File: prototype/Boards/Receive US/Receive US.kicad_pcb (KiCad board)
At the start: 2 copper layers, 37.1 x 26 mm, 37 parts, among them J1 Header, Q1 BC848BLT3G, U1 TLV9052SIDGSR, U2 TLV9052SIDGSR

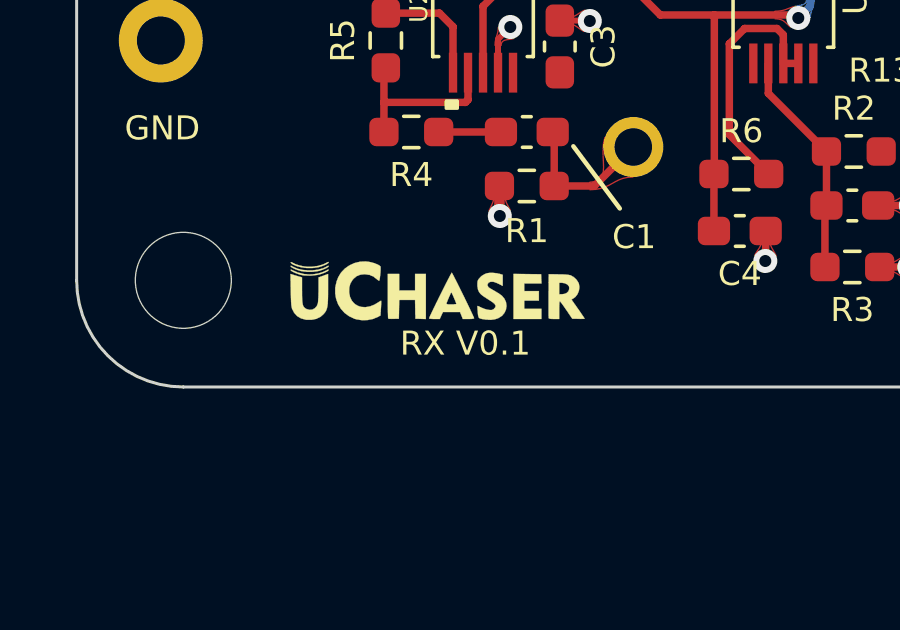
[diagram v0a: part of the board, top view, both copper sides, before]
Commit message: Update logo on receiver board; add new logo footprint & symbol
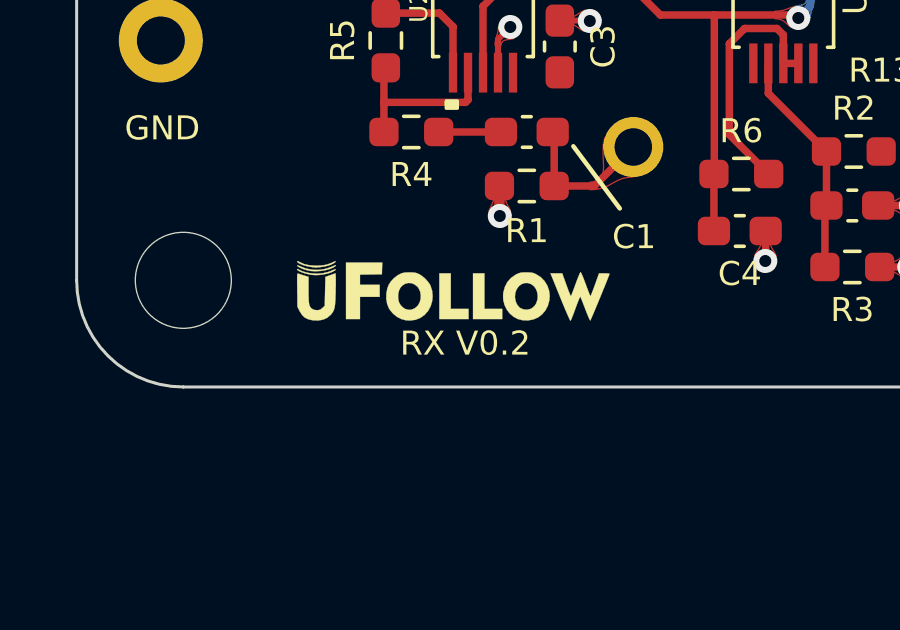
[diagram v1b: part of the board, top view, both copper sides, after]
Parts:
- removed Ref**: Val**, uFinder:logo
- added L1: ~, uFinder:uFollowLogo, F.Cu at (95.8, 109.5)
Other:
- board text added: "RX V0.2"
- board text removed: "RX V0.1"

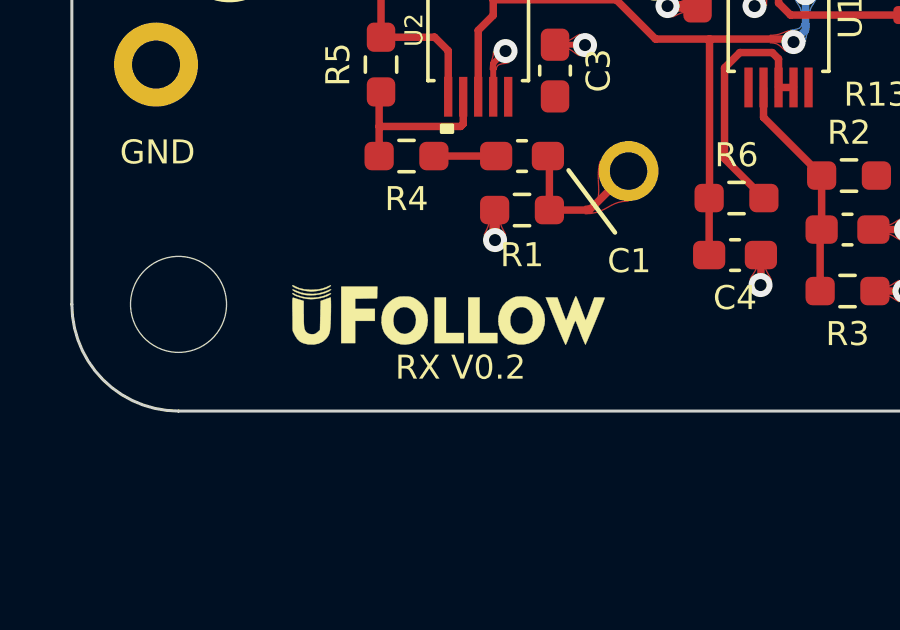
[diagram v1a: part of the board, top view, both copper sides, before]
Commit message: Adjustments to new logo
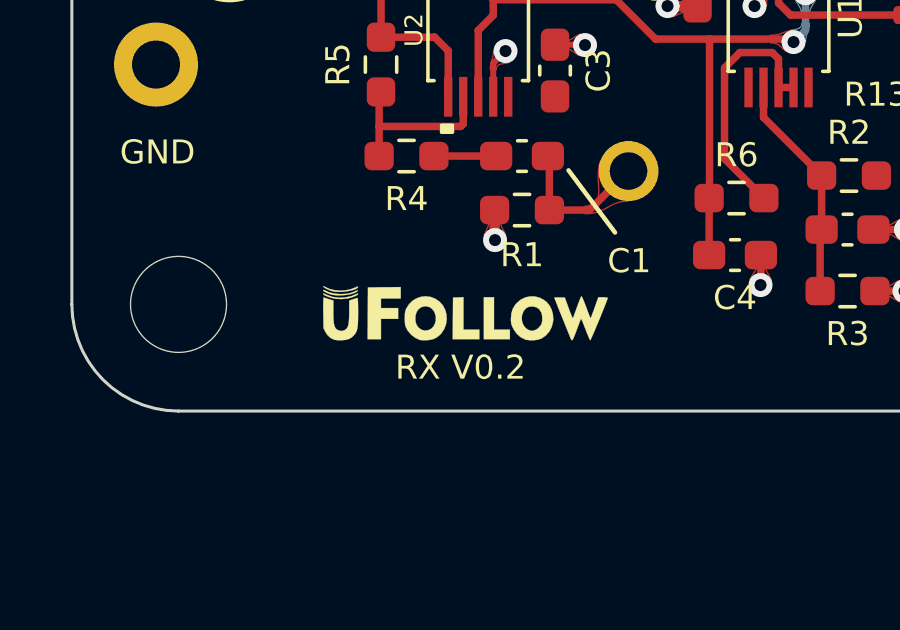
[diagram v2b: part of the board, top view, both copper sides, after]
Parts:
- moved L1 6.10 mm to (89.8, 108.8)
